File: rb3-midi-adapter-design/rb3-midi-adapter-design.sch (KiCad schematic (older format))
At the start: 1 part

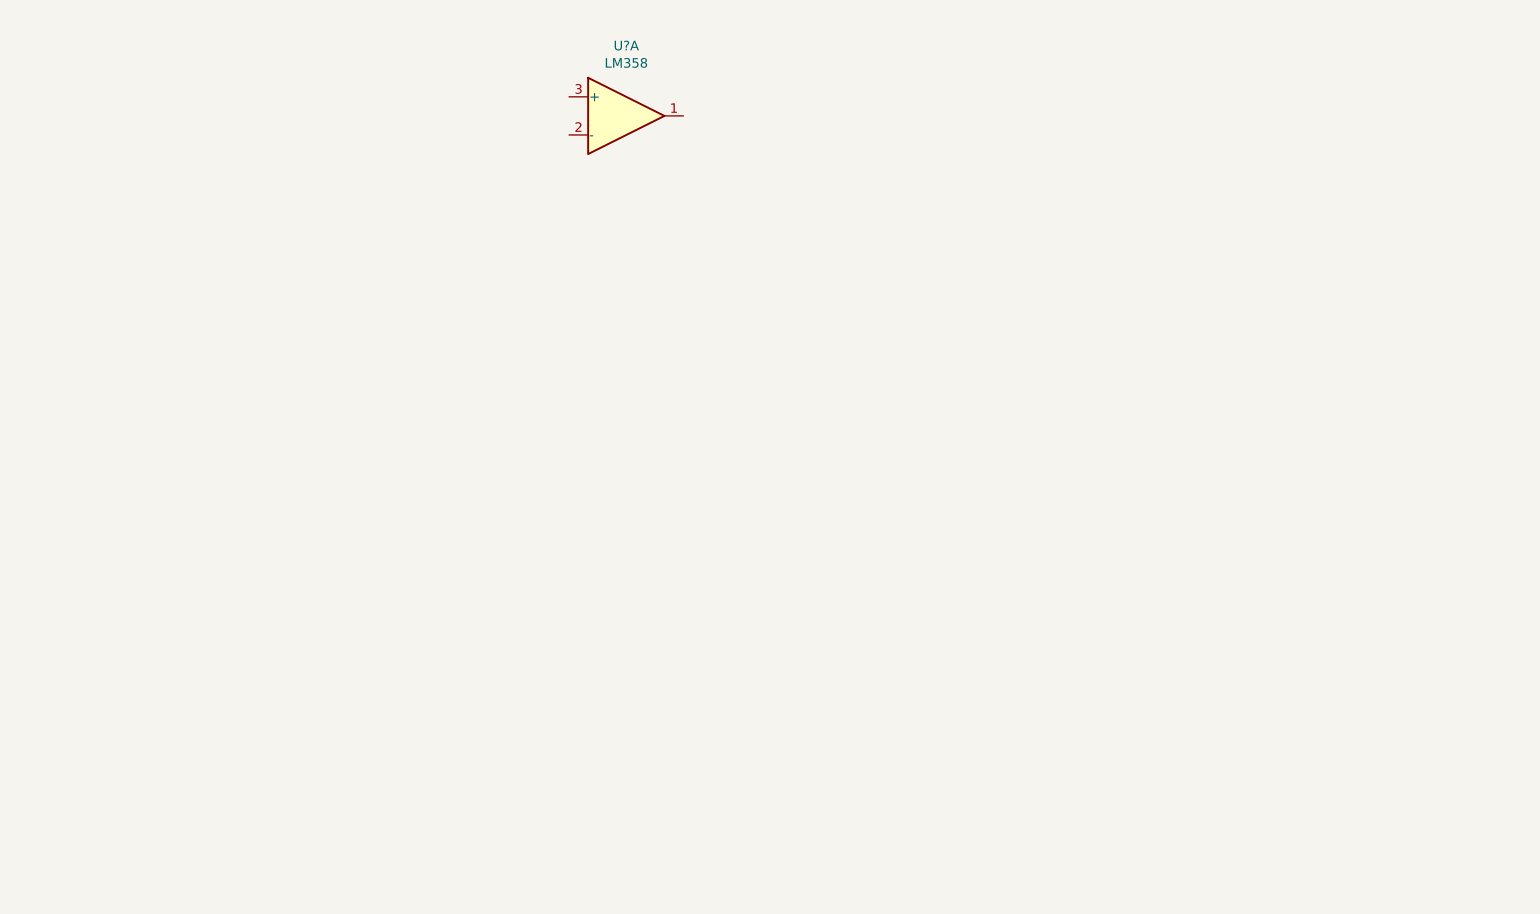
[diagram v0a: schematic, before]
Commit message: Start work on adapter schematics and PCB
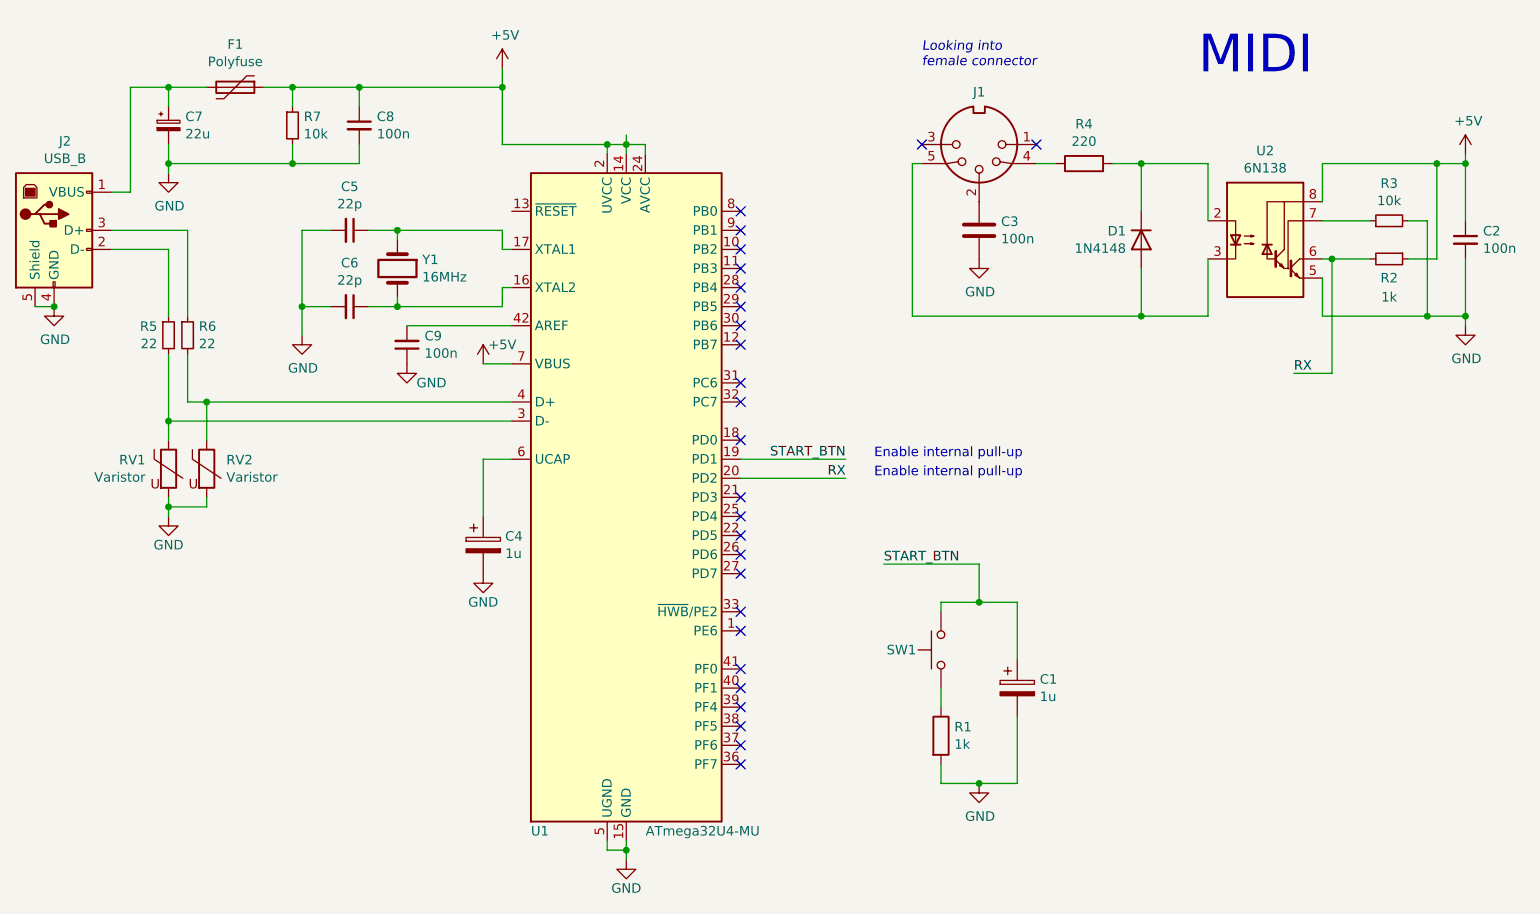
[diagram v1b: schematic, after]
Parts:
- removed U?: LM358, symbol Amplifier_Operational:LM358
- added C1, C4: 1u, Capacitor_THT:CP_Radial_D4.0mm_P1.50mm, symbol Device:CP
- added C2, C8, C9: 100n, Capacitor_THT:C_Disc_D3.0mm_W1.6mm_P2.50mm, symbol Device:C_Small
- added C3: 100n, Capacitor_THT:C_Disc_D3.0mm_W1.6mm_P2.50mm, symbol Device:C
- added C5, C6: 22p, Capacitor_THT:C_Disc_D3.0mm_W1.6mm_P2.50mm, symbol Device:C_Small
- added C7: 22u, Capacitor_THT:CP_Radial_D5.0mm_P2.00mm, symbol Device:CP_Small
- added D1: 1N4148, Diode_THT:D_DO-35_SOD27_P7.62mm_Horizontal, symbol Diode:1N4148
- added F1: Polyfuse, symbol Device:Polyfuse
- added J1: DIN-5_180degree, Eurocad:MIDI_DIN5, symbol Connector:DIN-5_180degree
- added J2: USB_B, Connector_USB:USB_B_OST_USB-B1HSxx_Horizontal, symbol Connector:USB_B
- added R1: 1k, Resistor_THT:R_Axial_DIN0204_L3.6mm_D1.6mm_P5.08mm_Horizontal, symbol Device:R
- added R2: 1k, Resistor_THT:R_Axial_DIN0204_L3.6mm_D1.6mm_P5.08mm_Horizontal, symbol Device:R_Small
- added R3, R7: 10k, Resistor_THT:R_Axial_DIN0204_L3.6mm_D1.6mm_P5.08mm_Horizontal, symbol Device:R_Small
- added R4: 220, Resistor_THT:R_Axial_DIN0204_L3.6mm_D1.6mm_P5.08mm_Horizontal, symbol Device:R
- added R5, R6: 22, Resistor_THT:R_Axial_DIN0204_L3.6mm_D1.6mm_P5.08mm_Horizontal, symbol Device:R_Small
- added RV1, RV2: Varistor, symbol Device:Varistor
- added SW1: SW_Push, Button_Switch_THT:SW_PUSH_6mm_H8mm, symbol Switch:SW_Push
- added U1: ATmega32U4-MU, Package_QFP:TQFP-44_10x10mm_P0.8mm, symbol MCU_Microchip_ATmega:ATmega32U4-MU
- added U2: 6N138, Package_DIP:DIP-8_W7.62mm_LongPads, symbol Isolator:6N138
- added Y1: 16MHz, Crystal:Crystal_HC49-4H_Vertical, symbol Device:Crystal
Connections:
- new net: C6.1, U1.16 (XTAL2), Y1.2
- new net: C5.1, U1.17 (XTAL1), Y1.1
- new net: R5.2, RV1.1, U1.3 (D-)
- new net: R6.2, RV2.1, U1.4 (D+)
- new net: C9.2, U1.42 (AREF)
- new net: C4.1, U1.6 (UCAP)
- new net: R1.1, SW1.1
- new net: C3.1, J1.2
- new net: J1.4, R4.1
- new net: D1.2 (A), J1.5, U2.3 (C2)
- new net: D1.1 (K), R4.2, U2.2 (C1)
- new net: R3.1, U2.7 (VO1)
- new net: C7.1, F1.2, J2.1 (VBUS)
- new net: J2.2 (D-), R5.1
- new net: J2.3 (D+), R6.1
- new net +5V: C2.1, C8.1, F1.1, R2.1, R7.1, U1.14 (VCC), U1.2 (UVCC), U1.24 (AVCC), U1.34 (VCC), U1.44 (AVCC), U1.7 (VBUS), U2.8 (VCC)
- new net GND: C1.2, C2.2, C3.2, C4.2, C5.2, C6.2, C7.2, C8.2, C9.1, J2.4 (GND), J2.5 (Shield), R1.2, R3.2, R7.2, RV1.2, RV2.2, U1.15 (GND), U1.23 (GND), U1.35 (GND), U1.43 (GND), U1.45 (GND), U1.5 (UGND), U2.5 (GND)
- new net RX: R2.2, U1.20 (PD2), U2.6 (VO2)
- new net START_BTN: C1.1, SW1.2, U1.19 (PD1)
- no-connect marks 0 -> 26
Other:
- note added: "Enable internal pull-up"
- note added: "Looking into\nfemale connector"
- note added: "MIDI"
